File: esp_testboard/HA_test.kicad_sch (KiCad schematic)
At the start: 79 parts

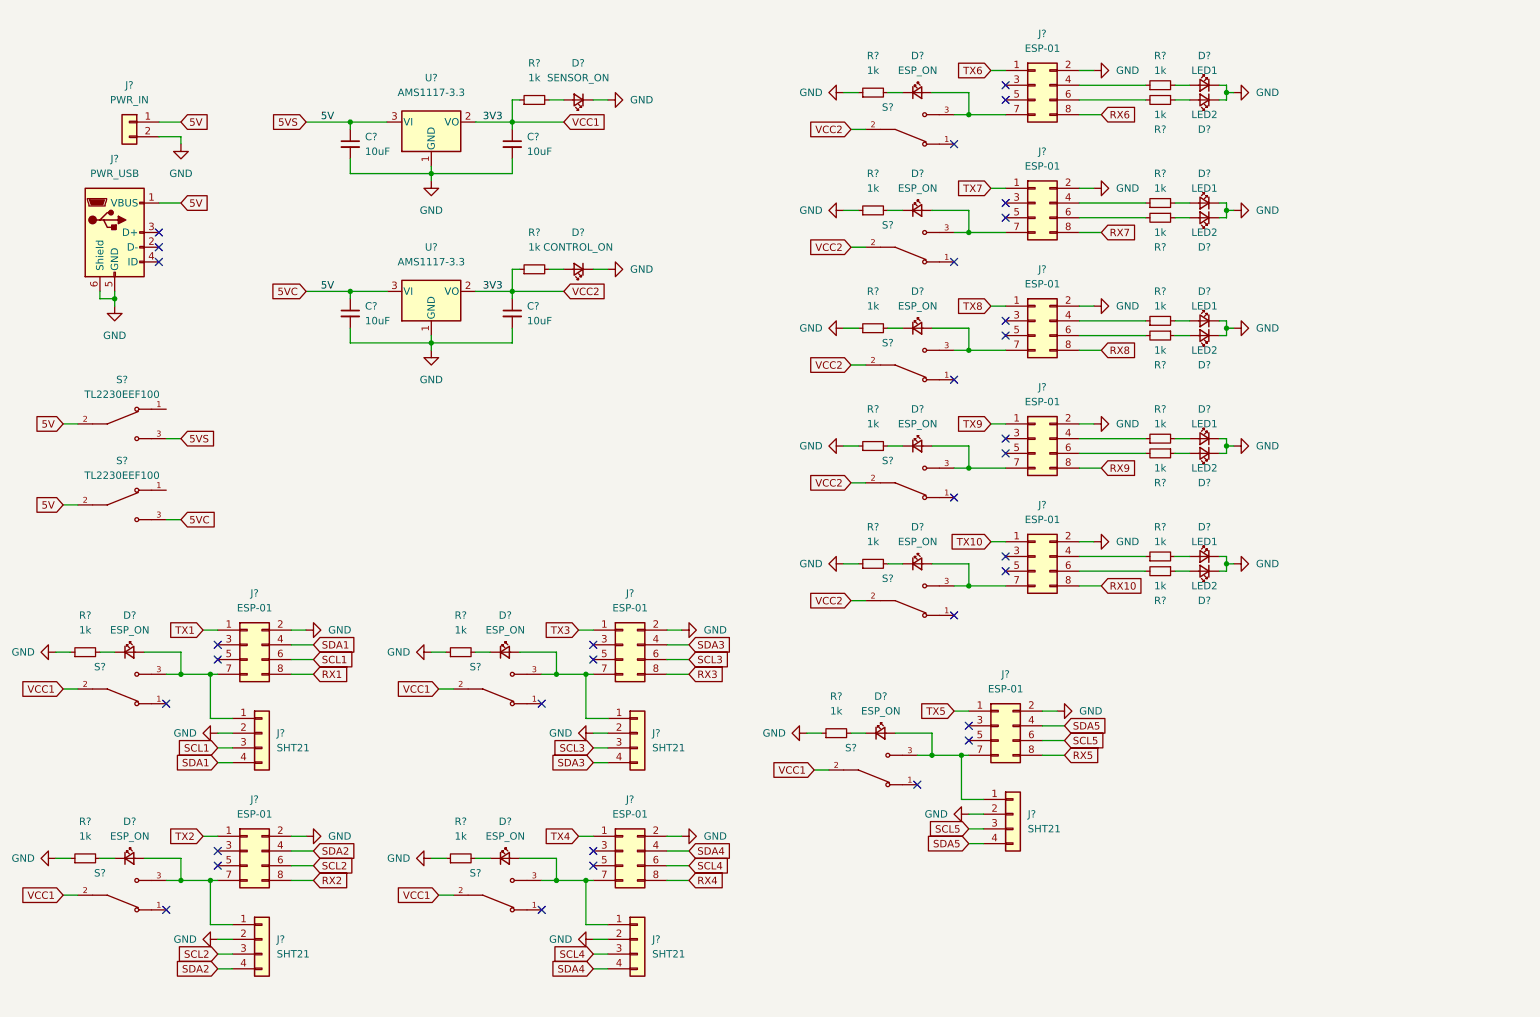
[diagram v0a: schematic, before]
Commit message: schematic and PCB for ESP tester
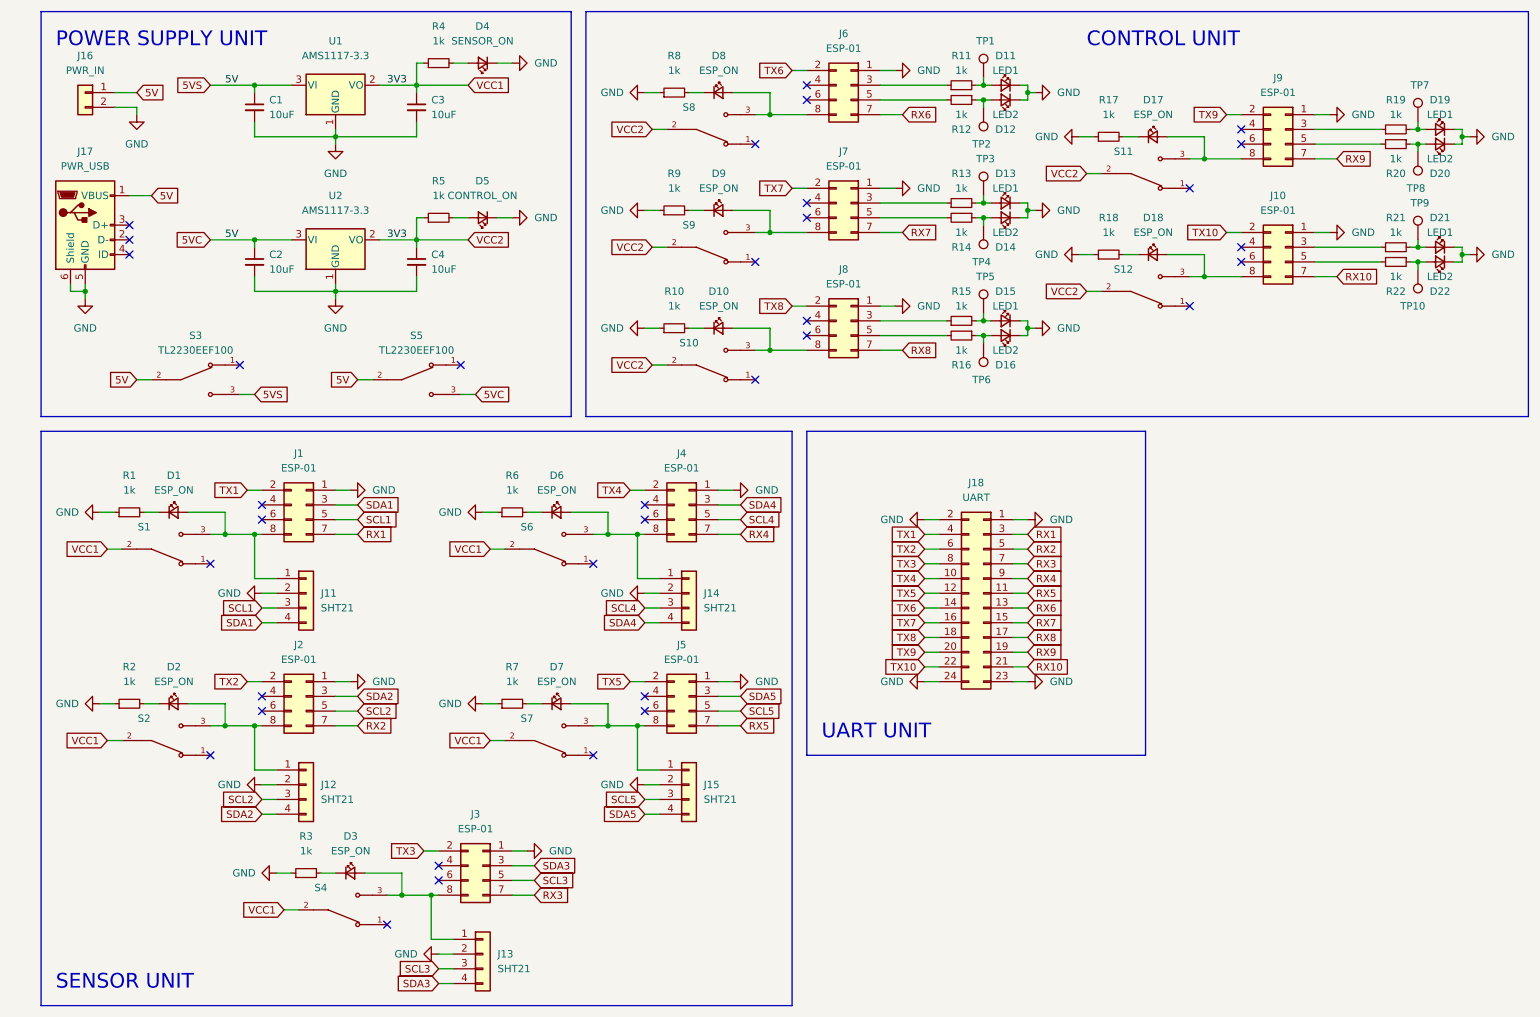
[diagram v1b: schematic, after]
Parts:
- added J18: UART, Connector_PinSocket_2.54mm:PinSocket_2x12_P2.54mm_Vertical, symbol Connector_Generic:Conn_02x12_Odd_Even
- added TP1, TP10, TP2, TP3, TP4, TP5, TP6, TP7, TP8, TP9: (no value), Connector_PinHeader_2.54mm:PinHeader_1x01_P2.54mm_Vertical, symbol Connector:TestPoint
- C1, C2, C3, C4: renamed from C?; footprint (none) -> Capacitor_SMD:C_1206_3216Metric
- D1, D10, D11, D12, D13, D14, D15, D16, D17, D18, D19, D2, D20, D21, D22, D3, D4, D5, D6, D7, D8, D9: renamed from D?; footprint (none) -> LED_SMD:LED_1206_3216Metric
- J1, J10, J2, J3, J4, J5, J6, J7, J8, J9: renamed from J?; footprint (none) -> Connector_PinSocket_2.54mm:PinSocket_2x04_P2.54mm_Vertical
- J11, J12, J13, J14, J15: renamed from J?; footprint (none) -> Connector_PinSocket_2.54mm:PinSocket_1x04_P2.54mm_Vertical
- J16: renamed from J?; footprint (none) -> Connector_JST:JST_XA_B02B-XASK-1-A_1x02_P2.50mm_Vertical
- J17: renamed from J?; footprint (none) -> PJ:USB_WE_629105150521
- R1, R10, R11, R12, R13, R14, R15, R16, R17, R18, R19, R2, R20, R21, R22, R3, R4, R5, R6, R7, R8, R9: renamed from R?; footprint (none) -> Resistor_SMD:R_1206_3216Metric
- S1, S10, S11, S12, S2, S3, S4, S5, S6, S7, S8, S9: renamed from S?; footprint SW_TL2230EEF100 -> PJ:SW_TL2230EEF100
- gave numbers to parts that had none: 2
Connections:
- net GND: now also J1.1 (Pin_1), J10.1 (Pin_1), J2.1 (Pin_1), J3.1 (Pin_1), J4.1 (Pin_1), J5.1 (Pin_1), J6.1 (Pin_1), J7.1 (Pin_1), J8.1 (Pin_1), J9.1 (Pin_1), J18.1 (Pin_1), J18.2 (Pin_2), J18.23 (Pin_23), J18.24 (Pin_24); no longer J1.2 (Pin_2), J10.2 (Pin_2), J2.2 (Pin_2), J3.2 (Pin_2), J4.2 (Pin_2), J5.2 (Pin_2), J6.2 (Pin_2), J7.2 (Pin_2), J8.2 (Pin_2), J9.2 (Pin_2)
- net RX1: now also J1.7 (Pin_7), J18.3 (Pin_3); no longer J1.8 (Pin_8)
- net RX10: now also J10.7 (Pin_7), J18.21 (Pin_21); no longer J10.8 (Pin_8)
- net RX2: now also J2.7 (Pin_7), J18.5 (Pin_5); no longer J2.8 (Pin_8)
- net RX3: now also J3.7 (Pin_7), J18.7 (Pin_7); no longer J3.8 (Pin_8)
- net RX4: now also J4.7 (Pin_7), J18.9 (Pin_9); no longer J4.8 (Pin_8)
- net RX5: now also J5.7 (Pin_7), J18.11 (Pin_11); no longer J5.8 (Pin_8)
- net RX6: now also J6.7 (Pin_7), J18.13 (Pin_13); no longer J6.8 (Pin_8)
- net RX7: now also J7.7 (Pin_7), J18.15 (Pin_15); no longer J7.8 (Pin_8)
- net RX8: now also J8.7 (Pin_7), J18.17 (Pin_17); no longer J8.8 (Pin_8)
- net RX9: now also J9.7 (Pin_7), J18.19 (Pin_19); no longer J9.8 (Pin_8)
- net SCL1: now also J1.5 (Pin_5); no longer J1.6 (Pin_6)
- net SCL2: now also J2.5 (Pin_5); no longer J2.6 (Pin_6)
- net SCL3: now also J3.5 (Pin_5); no longer J3.6 (Pin_6)
- net SCL4: now also J4.5 (Pin_5); no longer J4.6 (Pin_6)
- net SCL5: now also J5.5 (Pin_5); no longer J5.6 (Pin_6)
- net SDA1: now also J1.3 (Pin_3); no longer J1.4 (Pin_4)
- net SDA2: now also J2.3 (Pin_3); no longer J2.4 (Pin_4)
- net SDA3: now also J3.3 (Pin_3); no longer J3.4 (Pin_4)
- net SDA4: now also J4.3 (Pin_3); no longer J4.4 (Pin_4)
- net SDA5: now also J5.3 (Pin_3); no longer J5.4 (Pin_4)
- net TX1: now also J1.2 (Pin_2), J18.4 (Pin_4); no longer J1.1 (Pin_1)
- net TX10: now also J10.2 (Pin_2), J18.22 (Pin_22); no longer J10.1 (Pin_1)
- net TX2: now also J2.2 (Pin_2), J18.6 (Pin_6); no longer J2.1 (Pin_1)
- net TX3: now also J3.2 (Pin_2), J18.8 (Pin_8); no longer J3.1 (Pin_1)
- net TX4: now also J4.2 (Pin_2), J18.10 (Pin_10); no longer J4.1 (Pin_1)
- net TX5: now also J5.2 (Pin_2), J18.12 (Pin_12); no longer J5.1 (Pin_1)
- net TX6: now also J6.2 (Pin_2), J18.14 (Pin_14); no longer J6.1 (Pin_1)
- net TX7: now also J7.2 (Pin_2), J18.16 (Pin_16); no longer J7.1 (Pin_1)
- net TX8: now also J8.2 (Pin_2), J18.18 (Pin_18); no longer J8.1 (Pin_1)
- net TX9: now also J9.2 (Pin_2), J18.20 (Pin_20); no longer J9.1 (Pin_1)
- net at D2.2 (A), J12.1 (Pin_1), S2.3: now also J2.8 (Pin_8); no longer J2.7 (Pin_7)
- net at D18.2 (A), S12.3: now also J10.8 (Pin_8); no longer J10.7 (Pin_7)
- net at D20.2 (A), R20.1: now also TP8.1
- net at R20.2: now also J9.5 (Pin_5); no longer J9.6 (Pin_6)
- net at D6.2 (A), J14.1 (Pin_1), S6.3: now also J4.8 (Pin_8); no longer J4.7 (Pin_7)
- net at D1.2 (A), J11.1 (Pin_1), S1.3: now also J1.8 (Pin_8); no longer J1.7 (Pin_7)
- net at D15.2 (A), R15.2: now also TP5.1
- net at D21.2 (A), R21.2: now also TP9.1
- net at D10.2 (A), S10.3: now also J8.8 (Pin_8); no longer J8.7 (Pin_7)
- net at D8.2 (A), S8.3: now also J6.8 (Pin_8); no longer J6.7 (Pin_7)
- net at D14.2 (A), R14.1: now also TP4.1
- net at D7.2 (A), J15.1 (Pin_1), S7.3: now also J5.8 (Pin_8); no longer J5.7 (Pin_7)
- net at D3.2 (A), J13.1 (Pin_1), S4.3: now also J3.8 (Pin_8); no longer J3.7 (Pin_7)
- net at D17.2 (A), S11.3: now also J9.8 (Pin_8); no longer J9.7 (Pin_7)
- net at D22.2 (A), R22.1: now also TP10.1
- net at R22.2: now also J10.5 (Pin_5); no longer J10.6 (Pin_6)
- net at D16.2 (A), R16.1: now also TP6.1
- net at R16.2: now also J8.5 (Pin_5); no longer J8.6 (Pin_6)
- net at R15.1: now also J8.3 (Pin_3); no longer J8.4 (Pin_4)
- net at D11.2 (A), R11.2: now also TP1.1
- net at J6.3 (Pin_3): now also R11.1
- net at J6.4 (Pin_4): no longer R11.1
- net at J6.5 (Pin_5): now also R12.2
- net at J6.6 (Pin_6): no longer R12.2
- net at R14.2: now also J7.5 (Pin_5); no longer J7.6 (Pin_6)
- net at D12.2 (A), R12.1: now also TP2.1
- net at D9.2 (A), S9.3: now also J7.8 (Pin_8); no longer J7.7 (Pin_7)
- net at R21.1: now also J10.3 (Pin_3); no longer J10.4 (Pin_4)
- net at R13.1: now also J7.3 (Pin_3); no longer J7.4 (Pin_4)
- net at D13.2 (A), R13.2: now also TP3.1
- net at J9.3 (Pin_3): now also R19.1
- net at J9.4 (Pin_4): no longer R19.1
- net at D19.2 (A), R19.2: now also TP7.1
- no-connect marks 33 -> 35
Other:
- note added: "CONTROL UNIT"
- note added: "POWER SUPPLY UNIT"
- note added: "SENSOR UNIT"
- note added: "UART UNIT"
- moved on the sheet: C1, C2, C3, C4, D1, D10, D11, D12, D13, D14, D15, D16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

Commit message: schematic and PCB for ESP tester
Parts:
- added C10, C11, C12, C13, C14, C15, C16, C5, C6, C7: 100nF, Capacitor_SMD:C_1206_3216Metric, symbol Device:C_Small
- added C8, C9: 47uF/6.3V, PJ:CAPAE430X550N, symbol Device:C_Polarized_Small
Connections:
- net 5V: no longer C1.1, C2.1, S3.3, S5.3, U1.3 (VI), U2.3 (VI)
- net GND: now also C10.2, C11.2, C12.2, C13.2, C14.2, C15.2, C16.2, C5.2, C6.2, C7.2, C8.2, C9.2
- net VCC1: now also C8.1; no longer C4.1, R5.1, S10.2, S11.2, S12.2, S8.2, S9.2, U2.2 (VO)
- net at D2.2 (A), J12.1 (Pin_1), J2.8 (Pin_8)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: now also C6.1
- net at D18.2 (A), J10.8 (Pin_8), S12.3: now also C16.1
- net at D6.2 (A), J14.1 (Pin_1), J4.8 (Pin_8)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: now also C10.1
- net at D1.2 (A), J1.8 (Pin_8), J11.1 (Pin_1)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: now also C5.1
- net at D10.2 (A), J8.8 (Pin_8), S10.3: now also C14.1
- net at D8.2 (A), J6.8 (Pin_8), S8.3: now also C12.1
- net at D7.2 (A), J15.1 (Pin_1), J5.8 (Pin_8)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: now also C11.1
- net at D3.2 (A), J13.1 (Pin_1), J3.8 (Pin_8)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: now also C7.1
- net at D17.2 (A), J9.8 (Pin_8), S11.3: now also C15.1
- net at D9.2 (A), J7.8 (Pin_8), S9.3: now also C13.1
- new net 5VC: C2.1, S5.3, U2.3 (VI)
- new net 5VS: C1.1, S3.3, U1.3 (VI)
- new net VCC2: C4.1, C9.1, R5.1, S10.2, S11.2, S12.2, S8.2, S9.2, U2.2 (VO)

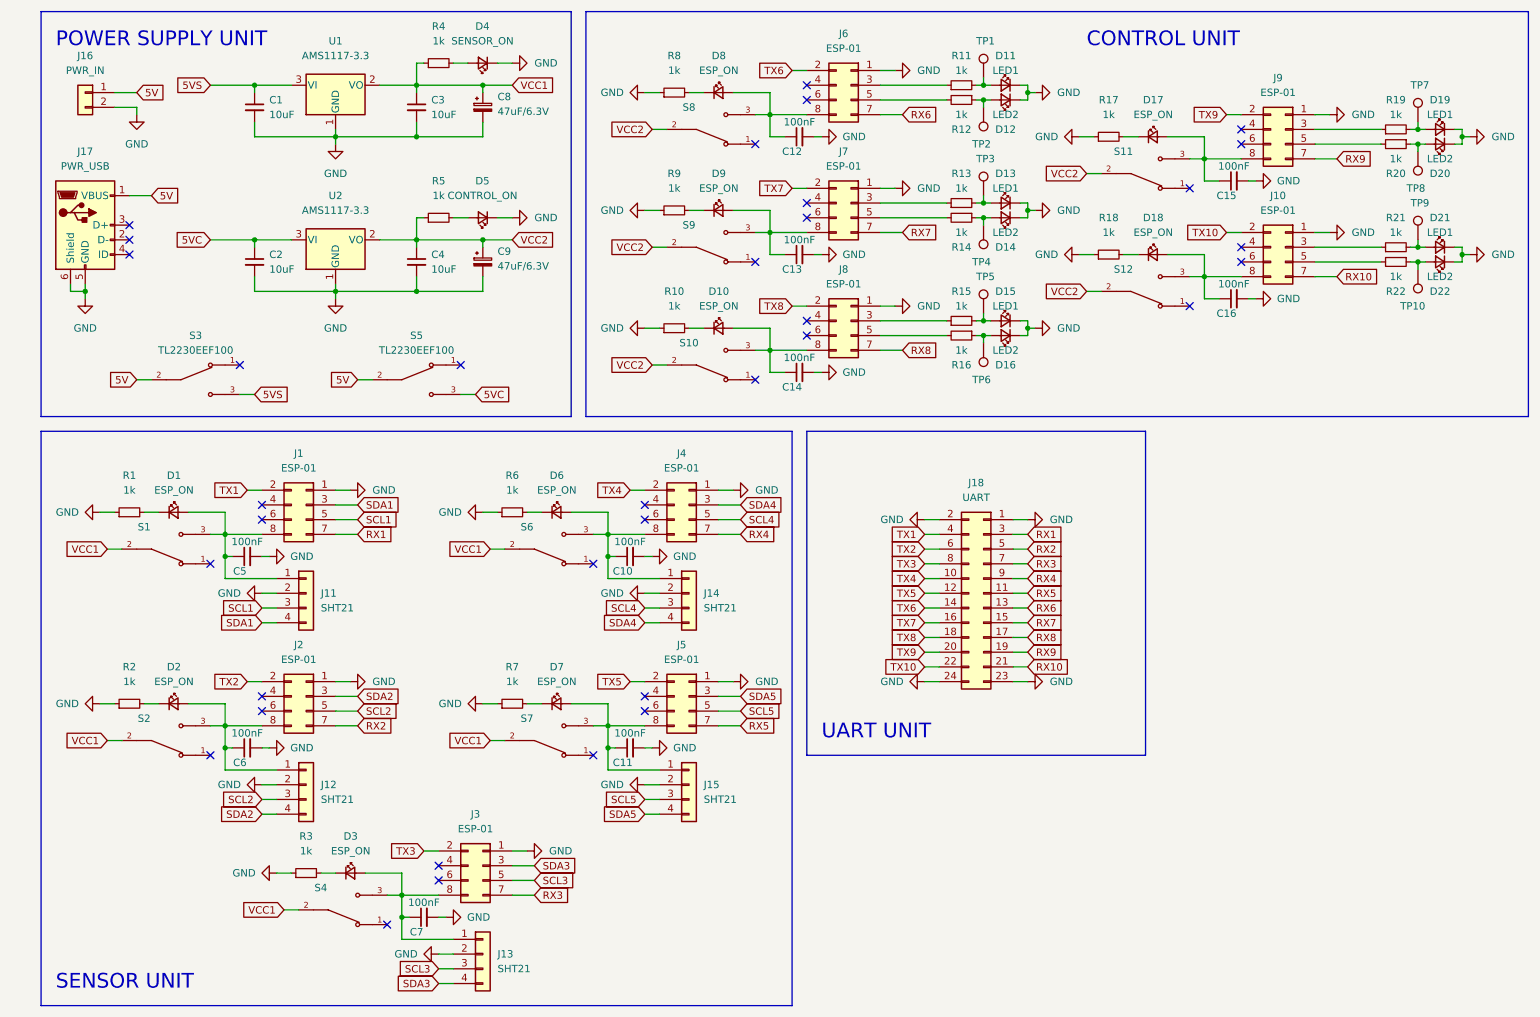
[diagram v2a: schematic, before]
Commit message: Micro USB upgraded to USB-C
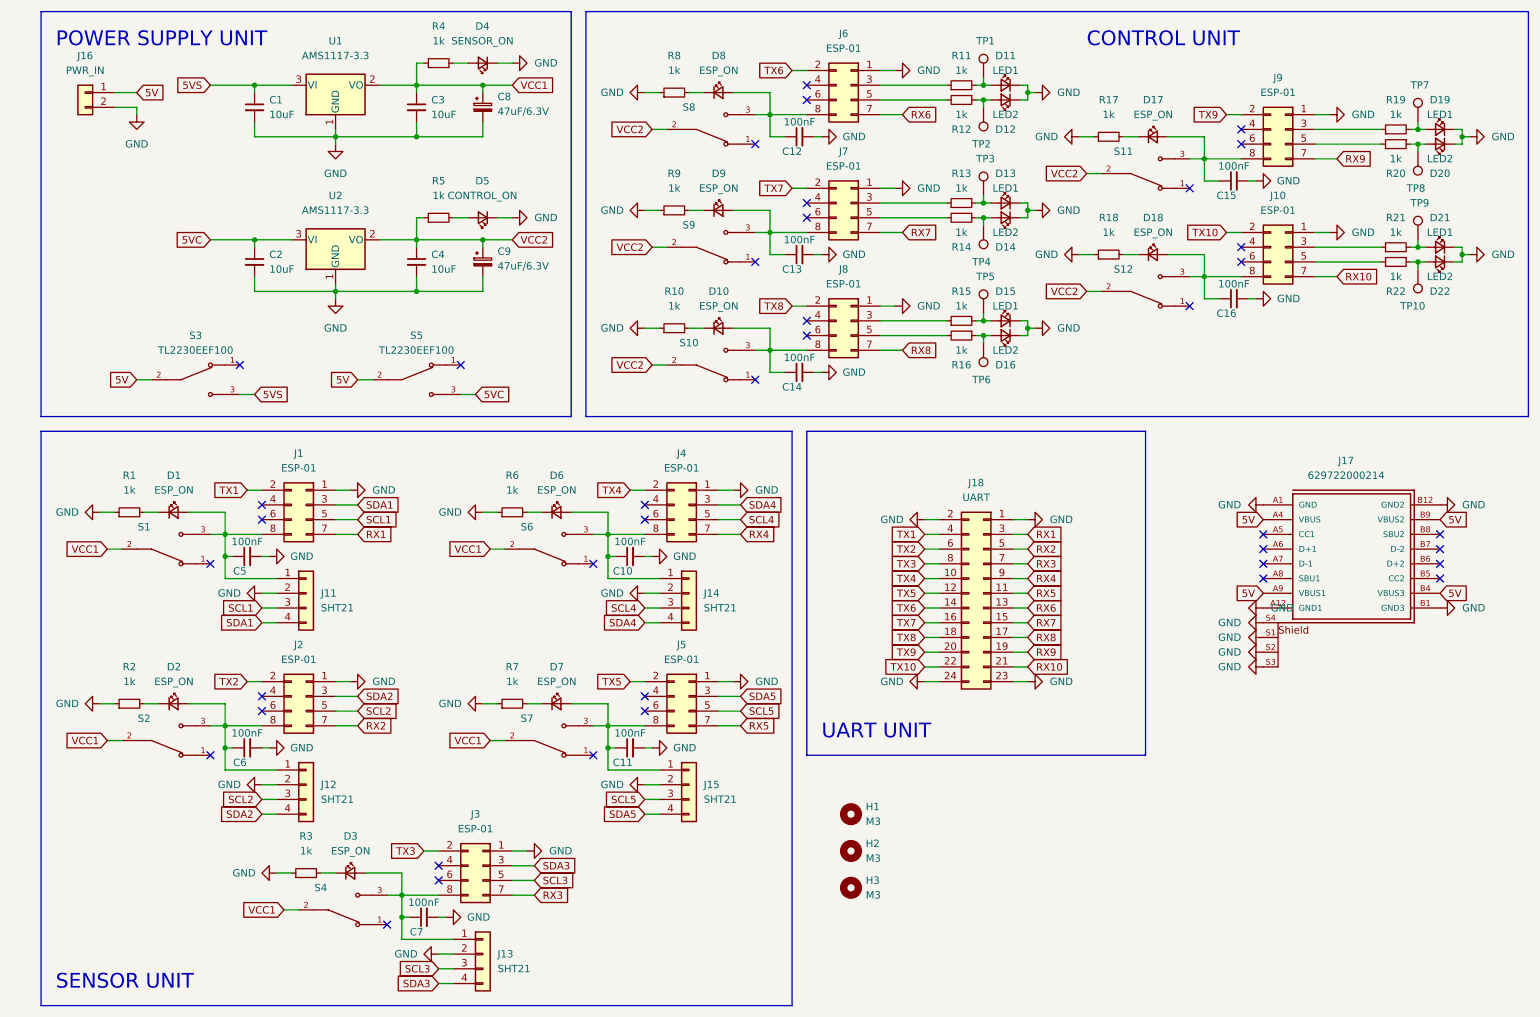
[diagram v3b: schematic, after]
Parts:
- removed J17: PWR_USB, PJ:USB_WE_629105150521, symbol Connector:USB_B_Micro
- added H1, H2, H3: M3, MountingHole:MountingHole_3.2mm_M3, symbol Mechanical:MountingHole
- added J17: 629722000214, PJ:629722000214, symbol PJ:629722000214
- J16: footprint Connector_JST:JST_XA_B02B-XASK-1-A_1x02_P2.50mm_Vertical -> PJ:68800211622
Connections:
- net 5V: now also J17.A4 (VBUS), J17.A9 (VBUS1), J17.B4 (VBUS3), J17.B9 (VBUS2)
- net GND: now also J17.A1 (GND), J17.A12 (GND1), J17.B1 (GND3), J17.B12 (GND2), J17.S1, J17.S2, J17.S3, J17.S4
- no-connect marks 35 -> 40
